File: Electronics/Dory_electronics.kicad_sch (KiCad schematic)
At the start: 20 parts, among them J1 Bateria 2S, J10 SHARP_CENTRO_E, J2 Conn_01x08, J3 Conn_01x08, J4 Motor B, J5 Motor A, J6 sensor IR, J7 VL53L0X_ESQUERDO, J8 SHARP_CENTRO_D, J9 VL53L0X_DIREITO, U1 LM1117 5V

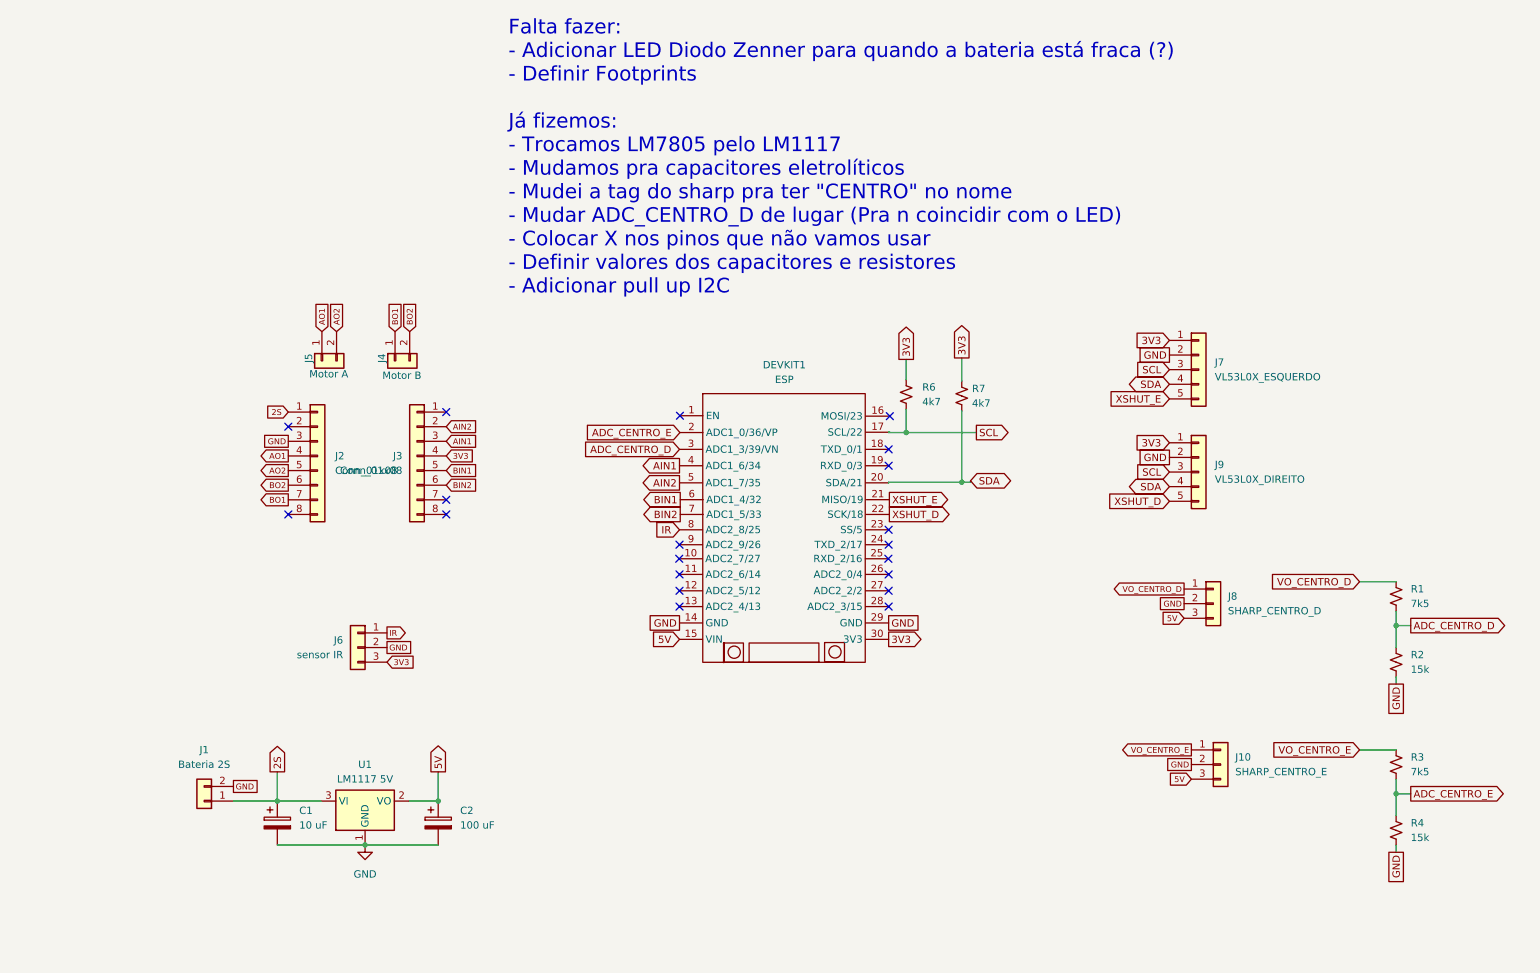
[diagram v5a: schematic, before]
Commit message: chore: add footprints to schematic
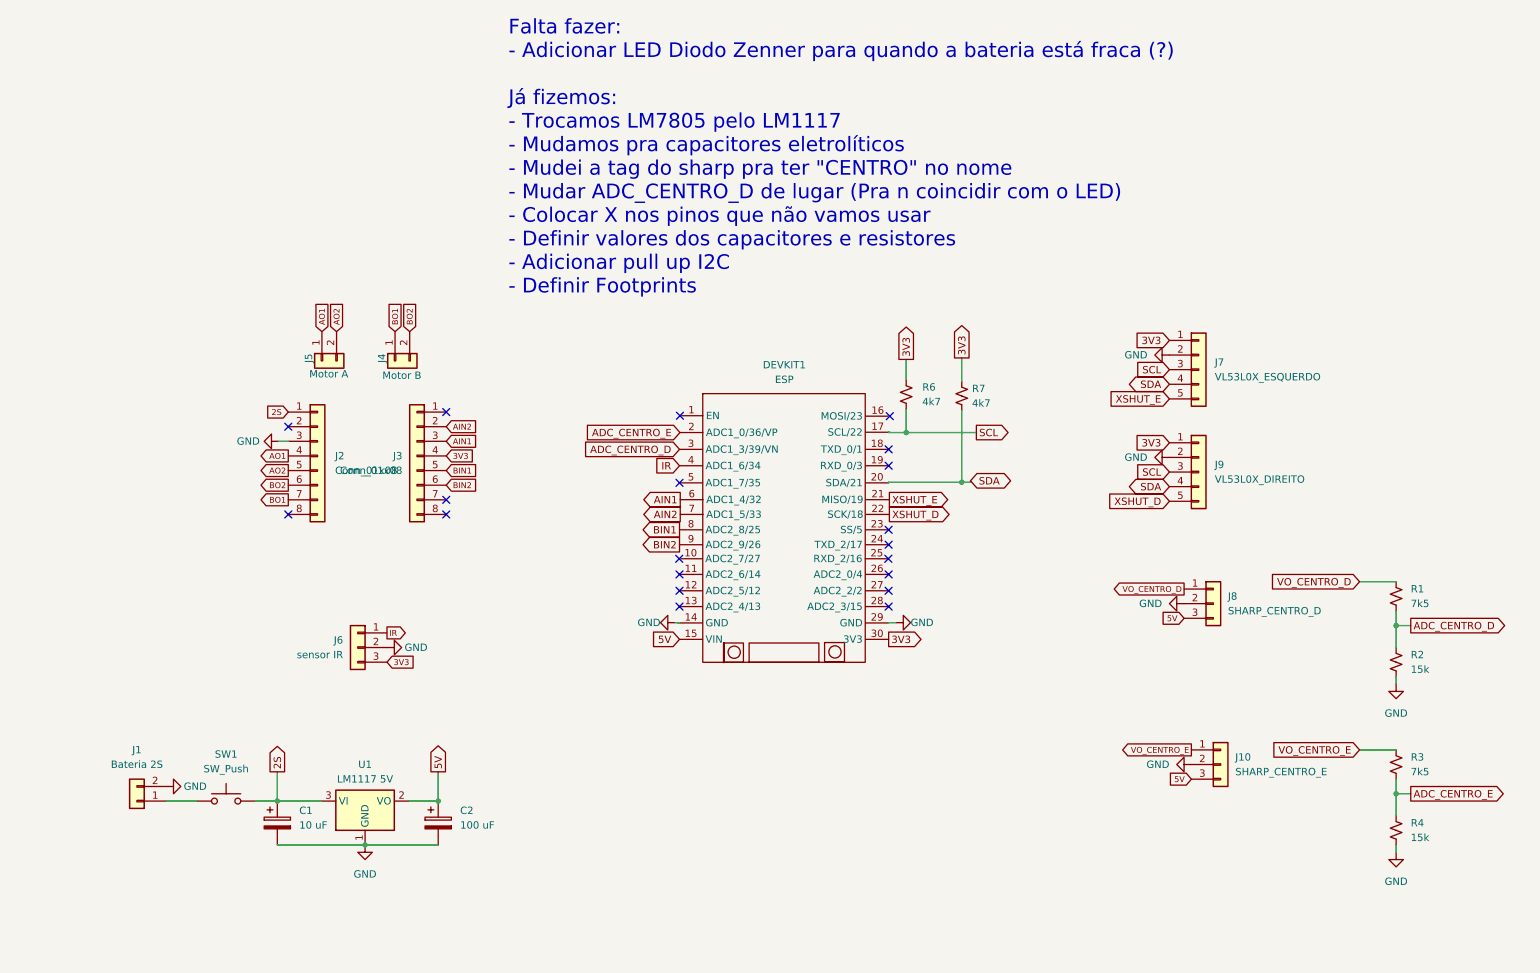
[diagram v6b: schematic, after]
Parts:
- added SW1: SW_Push, Button_Switch_THT:Nidec_Copal_SH-7010C, symbol Switch:SW_Push
- C1: footprint (none) -> Capacitor_THT:CP_Radial_D5.0mm_P2.50mm
- C2: footprint (none) -> Capacitor_THT:CP_Radial_D6.3mm_P2.50mm
- DEVKIT1: footprint (none) -> KIKAD bibliotecas:esp32_devkit_v1_doit
- J1: footprint (none) -> Connector_JST:JST_PH_B2B-PH-K_1x02_P2.00mm_Vertical
- J10, J8: footprint (none) -> Connector_PinSocket_2.54mm:PinSocket_1x03_P2.54mm_Vertical
- J2, J3: footprint (none) -> Connector_PinSocket_2.54mm:PinSocket_1x08_P2.54mm_Vertical
- J4, J5: footprint (none) -> Connector_JST:JST_XH_B2B-XH-AM_1x02_P2.50mm_Vertical
- J6: footprint (none) -> Connector_PinHeader_2.54mm:PinHeader_1x03_P2.54mm_Vertical
- J7, J9: footprint (none) -> Connector_JST:JST_XH_B5B-XH-AM_1x05_P2.50mm_Vertical
- R1, R2, R3, R4: footprint (none) -> Resistor_SMD:R_0805_2012Metric
- R6, R7: footprint (none) -> Resistor_THT:R_Axial_DIN0207_L6.3mm_D2.5mm_P10.16mm_Horizontal
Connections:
- net 2S: now also SW1.2; no longer J1.1 (Pin_1)
- net AIN1: now also DEVKIT1.6 (ADC1_4/32); no longer DEVKIT1.4 (ADC1_6/34)
- net AIN2: now also DEVKIT1.7 (ADC1_5/33); no longer DEVKIT1.5 (ADC1_7/35)
- net BIN1: now also DEVKIT1.8 (ADC2_8/25); no longer DEVKIT1.6 (ADC1_4/32)
- net BIN2: now also DEVKIT1.9 (ADC2_9/26); no longer DEVKIT1.7 (ADC1_5/33)
- net IR: now also DEVKIT1.4 (ADC1_6/34); no longer DEVKIT1.8 (ADC2_8/25)
- new net: J1.1 (Pin_1), SW1.1
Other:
- note added: "Falta fazer: - Adicionar LED Diodo Zenner para quando a bateria está fraca (?) Já fizemos: - Trocamos LM7805 pelo LM1117 - Mudamos pra capacitores eletrolíticos - Mudei a tag do sharp pra ter "CENTRO" no nome - Mudar ADC_CENTRO_D de lugar (Pra n coincidir com o LED) - Colocar X nos pinos que não vamos usar - Definir valores dos capacitores e resistores - Adicionar pull up I2C - Definir Footprints"
- note removed: "Falta fazer: - Adicionar LED Diodo Zenner para quando a bateria está fraca (?) - Definir Footprints Já fizemos: - Trocamos LM7805 pelo LM1117 - Mudamos pra capacitores eletrolíticos - Mudei a tag do sharp pra ter "CENTRO" no nome - Mudar ADC_CENTRO_D de lugar (Pra n coincidir com o LED) - Colocar X nos pinos que não vamos usar - Definir valores dos capacitores e resistores - Adicionar pull up I2C"
- moved on the sheet: J1

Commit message: chore(Electronics): organize and finish schematic
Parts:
- added R7: 15k, Resistor_SMD:R_0805_2012Metric, symbol Device:R_Small_US
- added R8: 7k5, Resistor_SMD:R_0805_2012Metric, symbol Device:R_Small_US
- DEVKIT1: footprint KIKAD bibliotecas:esp32_devkit_v1_doit -> esp32_devkit_v1_doit:esp32_devkit_v1_doit
- renumbered R6 to R5, R7 to R6
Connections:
- net 2S: now also R7.1
- net GND: now also R8.2
- net (2S)/3: now reaches DEVKIT1.5 (ADC1_7/35)
- net (2S)/3: now also R7.2, R8.1
- no-connect marks 20 -> 19
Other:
- note added: "Alimentação"
- note added: "Devkit Doit ESP32"
- note added: "InfraRed VS1838B"
- note added: "Motores"
- note added: "Ponte H"
- note added: "Sensores"
- note added: "Sharp 0A41SK - Sensores Distância Frontais"
- note added: "VL53L0X - Sensores Distância Laterais"
- note added: "Valida Tensão Bateria"
- note removed: "Falta fazer: - Adicionar LED Diodo Zenner para quando a bateria está fraca (?) Já fizemos: - Trocamos LM7805 pelo LM1117 - Mudamos pra capacitores eletrolíticos - Mudei a tag do sharp pra ter "CENTRO" no nome - Mudar ADC_CENTRO_D de lugar (Pra n coincidir com o LED) - Colocar X nos pinos que não vamos usar - Definir valores dos capacitores e resistores - Adicionar pull up I2C - Definir Footprints"
- moved on the sheet: C1, C2, DEVKIT1, J1, J10, J2, J3, J4, J5, J6, J7, J8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

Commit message: chore(Electronics): organize and finish schematic
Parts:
- removed J2, J3: Conn_01x08, Connector_PinSocket_2.54mm:PinSocket_1x08_P2.54mm_Vertical, symbol Connector_Generic:Conn_01x08
- removed SW1: SW_Push, Button_Switch_THT:Nidec_Copal_SH-7010C, symbol Switch:SW_Push
- added 6_Pins_Button1: ~, Button_Switch_THT:Nidec_Copal_SH-7010C, symbol esp32_devkit_v1_doit:Button_6_Pins
- added H_Bridge1: ~, esp32_devkit_v1_doit:H_Bridge, symbol esp32_devkit_v1_doit:H_Bridge
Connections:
- net 2S: now also 6_Pins_Button1.2 (O2), 6_Pins_Button1.4 (Output), H_Bridge1.1 (VM)
- net 3V3: now also DEVKIT1.16 (3V3), H_Bridge1.13 (STDBY); no longer DEVKIT1.30 (3V3)
- net ADC_CENTRO_E: now also DEVKIT1.4 (ADC1_6/34); no longer DEVKIT1.2 (ADC1_0/36/VP)
- net AIN1: now also DEVKIT1.8 (ADC2_8/25), H_Bridge1.14 (AIN1); no longer DEVKIT1.6 (ADC1_4/32)
- net AIN2: now also DEVKIT1.9 (ADC2_9/26), H_Bridge1.15 (AIN2); no longer DEVKIT1.7 (ADC1_5/33)
- net AO1: now also H_Bridge1.4 (AO1)
- net AO2: now also H_Bridge1.5 (AO2)
- net BIN1: now also DEVKIT1.7 (ADC1_5/33), H_Bridge1.12 (BIN1); no longer DEVKIT1.8 (ADC2_8/25)
- net BIN2: now also DEVKIT1.6 (ADC1_4/32), H_Bridge1.11 (BIN2); no longer DEVKIT1.9 (ADC2_9/26)
- net BO1: now also H_Bridge1.7 (BO1)
- net BO2: now also H_Bridge1.6 (BO2)
- net GND: now also DEVKIT1.17 (GND), H_Bridge1.3 (GND); no longer DEVKIT1.29 (GND)
- net IR: now also DEVKIT1.2 (ADC1_0/36/VP); no longer DEVKIT1.4 (ADC1_6/34)
- net SCL: now also DEVKIT1.29 (SCL/22); no longer DEVKIT1.17 (SCL/22)
- net SDA: now also DEVKIT1.26 (SDA/21); no longer DEVKIT1.20 (SDA/21)
- net XSHUT_D: now also DEVKIT1.24 (SCK/18); no longer DEVKIT1.22 (SCK/18)
- net XSHUT_E: now also DEVKIT1.25 (MISO/19); no longer DEVKIT1.21 (MISO/19)
- net at J1.1 (Pin_1): now also 6_Pins_Button1.C (Input)
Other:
- note removed: "Ponte H"
- moved on the sheet: C1, C2, J1, J5, U1
